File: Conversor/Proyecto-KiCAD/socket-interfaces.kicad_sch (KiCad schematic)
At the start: 24 parts, among them J7 DIMM100, P10 Header GPIO, P11 Header SD, P5 Header 7X2, P6 Header UART, P7 Header I2C, P8 Header PWM, P9 Header ADC, SW1 Switch, SW2 Switch, SW3 Switch, SW4 Switch

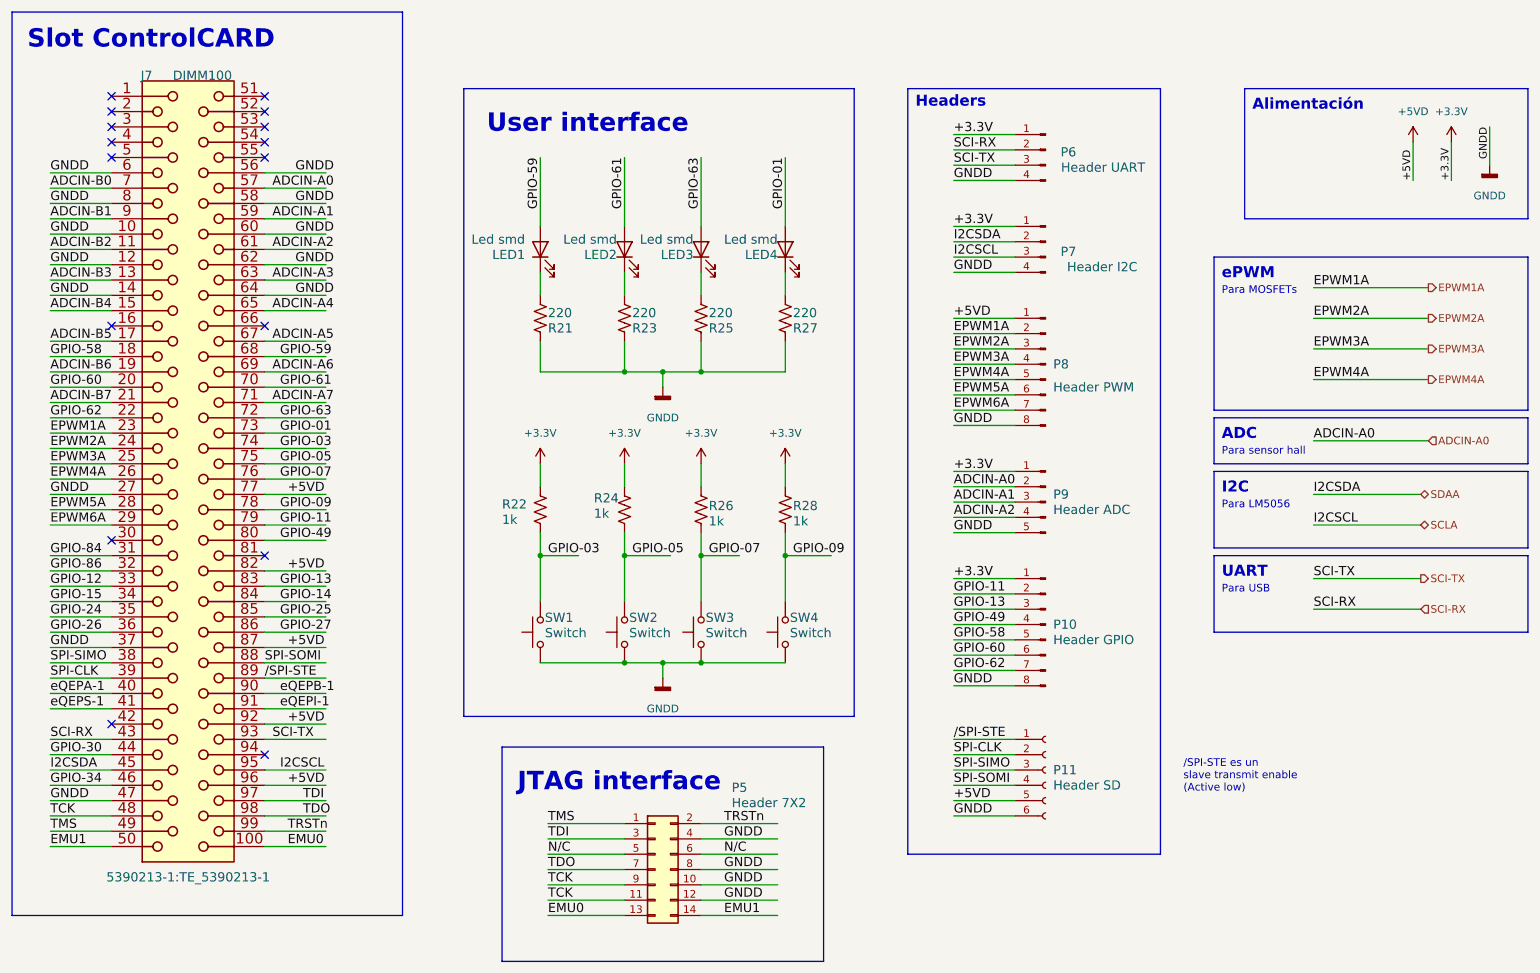
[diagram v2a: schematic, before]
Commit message: Reempezar el ordenado de componentes del PCB
- Intentar copiar mas a la placa adaptadora en la parte del DSP (digital)
  - Algunas cosas (como los headers y la parte de USB) se movieron para hacer entrar mejor las cosas
- Layout bastante completo
- Agregados algunos modelos 3D faltantes
Por hacer:
  - Mover y reorganizar la parte del LM5056, porque tiene una pata que va al secundario, y ahora esta muy lejos del area de GND2
  - Ver como reorganizar un poco para que no queden esquinas vacias
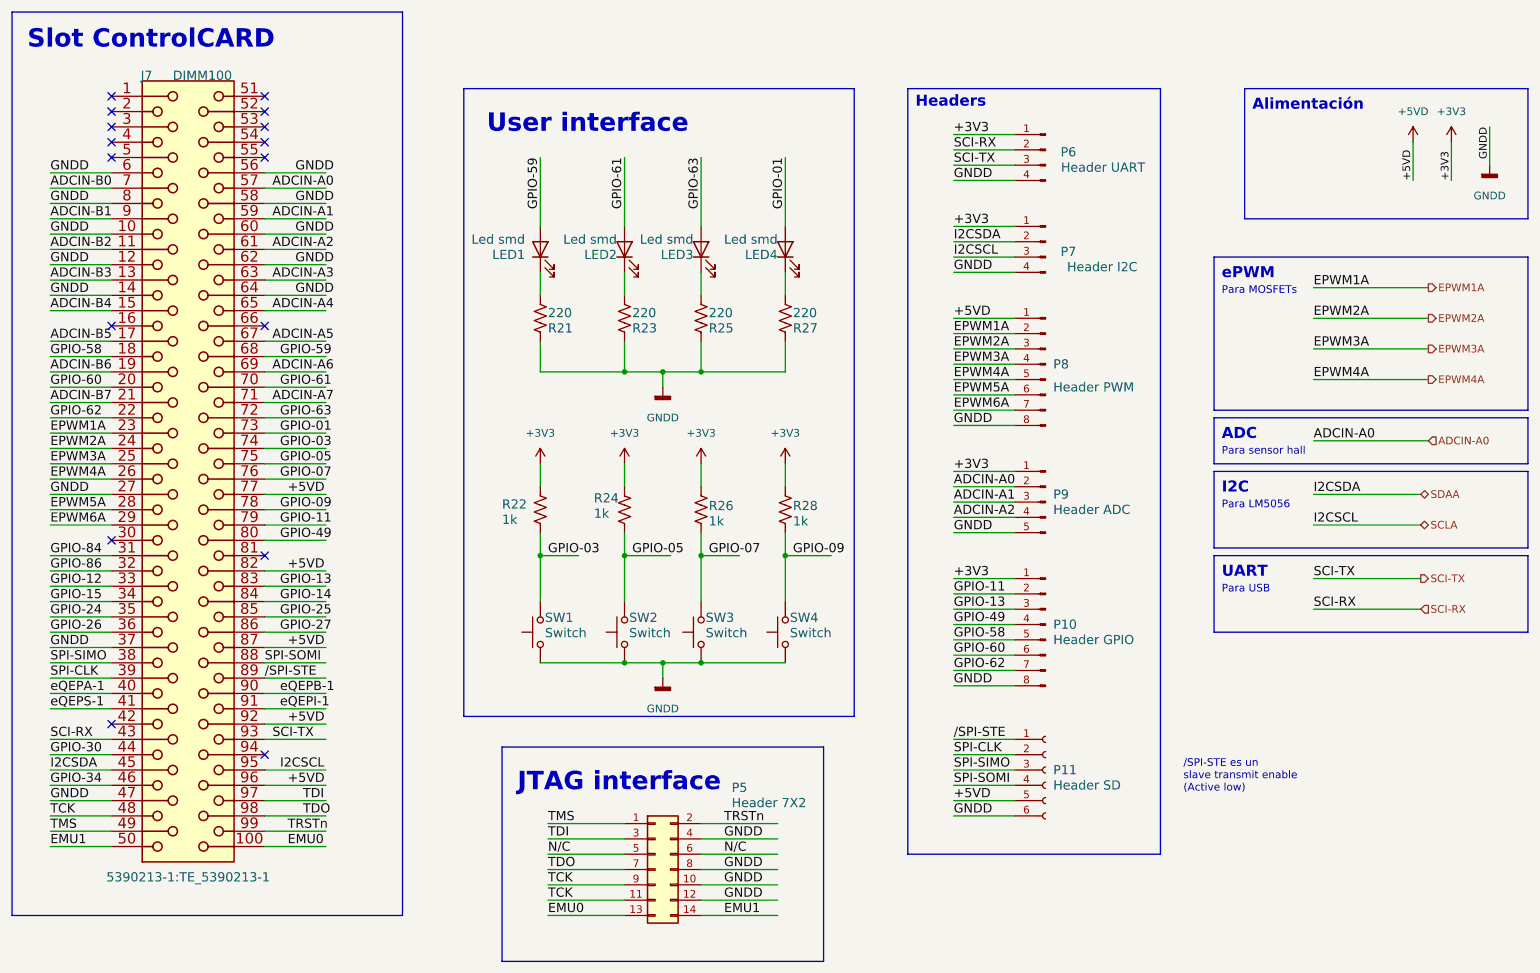
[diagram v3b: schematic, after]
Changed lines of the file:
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@@
     (effects (font (size 1.524 1.524)) (justify left bottom))
   )
-  (label "+3.3V" (at 175.26 91.44 0)
+  (label "+3V3" (at 175.26 91.44 0)
     (effects (font (size 1.524 1.524)) (justify left bottom))
   )
@@
     (effects (font (size 1.524 1.524)) (justify left bottom))
   )
-  (label "+3.3V" (at 175.26 35.56 0)
+  (label "+3V3" (at 175.26 35.56 0)
     (effects (font (size 1.524 1.524)) (justify left bottom))
   )
@@
     (effects (font (size 1.524 1.524)) (justify left bottom))
   )
-  (label "+3.3V" (at 175.26 109.22 0)
+  (label "+3V3" (at 175.26 109.22 0)
     (effects (font (size 1.524 1.524)) (justify left bottom))
   )
@@
     (effects (font (size 1.524 1.524)) (justify left bottom))
   )
-  (label "+3.3V" (at 257.81 43.18 90)
+  (label "+3V3" (at 257.81 43.18 90)
     (effects (font (size 1.27 1.27)) (justify left bottom))
   )
@@
     (effects (font (size 1.524 1.524)) (justify left bottom))
   )
-  (label "+3.3V" (at 175.26 50.8 0)
+  (label "+3V3" (at 175.26 50.8 0)
     (effects (font (size 1.524 1.524)) (justify left bottom))
   )
@@
     (effects (font (size 1.27 1.27)) (justify left))
   )
+  (symbol (lib_id "power:+3V3") (at 133.35 90.17 0) (unit 1)
+    (in_bom yes) (on_board yes) (fields_autoplaced)
+    (property "Reference" "#PWR0119" (id 0) (at 133.35 93.98 0)
+      (effects (font (size 1.27 1.27)) hide)
+    )
+    (property "Value" "+3V3" (id 1) (at 133.35 85.09 0))
+    (property "Footprint" "" (id 2) (at 133.35 90.17 0)
+      (effects (font (size 1.27 1.27)) hide)
+    )
+    (property "Datasheet" "" (id 3) (at 133.35 90.17 0)
+      (effects (font (size 1.27 1.27)) hide)
+    )
+    (pin "1")
+  )
   (symbol (lib_id "Device:R_US") (at 133.35 97.79 180) (unit 1)
     (in_bom yes) (on_board yes)
@@
     (pin "2")
   )
-  (symbol (lib_id "power:+3.3V") (at 120.65 90.17 0) (unit 1)
+  (symbol (lib_id "power:+3V3") (at 120.65 90.17 0) (unit 1)
     (in_bom yes) (on_board yes) (fields_autoplaced)
-    (property "Reference" "#PWR0121" (id 0) (at 120.65 93.98 0)
-      (effects (font (size 1.27 1.27)) hide)
-    )
-    (property "Value" "+3.3V" (id 1) (at 120.65 85.09 0))
+    (property "Reference" "#PWR0144" (id 0) (at 120.65 93.98 0)
+      (effects (font (size 1.27 1.27)) hide)
+    )
+    (property "Value" "+3V3" (id 1) (at 120.65 85.09 0))
     (property "Footprint" "" (id 2) (at 120.65 90.17 0)
       (effects (font (size 1.27 1.27)) hide)
@@
     (pin "9")
   )
+  (symbol (lib_id "power:+3V3") (at 147.32 90.17 0) (unit 1)
+    (in_bom yes) (on_board yes) (fields_autoplaced)
+    (property "Reference" "#PWR0121" (id 0) (at 147.32 93.98 0)
+      (effects (font (size 1.27 1.27)) hide)
+    )
+    (property "Value" "+3V3" (id 1) (at 147.32 85.09 0))
+    (property "Footprint" "" (id 2) (at 147.32 90.17 0)
+      (effects (font (size 1.27 1.27)) hide)
+    )
+    (property "Datasheet" "" (id 3) (at 147.32 90.17 0)
+      (effects (font (size 1.27 1.27)) hide)
+    )
+    (pin "1")
+  )
   (symbol (lib_id "Device:R_US") (at 106.68 66.04 0) (unit 1)
     (in_bom yes) (on_board yes)
@@
     (pin "1")
     (pin "2")
-  )
-  (symbol (lib_id "power:+3.3V") (at 106.68 90.17 0) (unit 1)
-    (in_bom yes) (on_board yes) (fields_autoplaced)
-    (property "Reference" "#PWR0122" (id 0) (at 106.68 93.98 0)
-      (effects (font (size 1.27 1.27)) hide)
-    )
-    (property "Value" "+3.3V" (id 1) (at 106.68 85.09 0))
-    (property "Footprint" "" (id 2) (at 106.68 90.17 0)
-      (effects (font (size 1.27 1.27)) hide)
-    )
-    (property "Datasheet" "" (id 3) (at 106.68 90.17 0)
-      (effects (font (size 1.27 1.27)) hide)
-    )
-    (pin "1")
   )
   (symbol (lib_id "Connector:Conn_01x06_Female") (at 190.5 140.97 0) (unit 1)
@@
     (pin "1")
   )
-  (symbol (lib_id "power:+3.3V") (at 147.32 90.17 0) (unit 1)
-    (in_bom yes) (on_board yes) (fields_autoplaced)
-    (property "Reference" "#PWR0118" (id 0) (at 147.32 93.98 0)
-      (effects (font (size 1.27 1.27)) hide)
-    )
-    (property "Value" "+3.3V" (id 1) (at 147.32 85.09 0))
-    (property "Footprint" "" (id 2) (at 147.32 90.17 0)
-      (effects (font (size 1.27 1.27)) hide)
-    )
-    (property "Datasheet" "" (id 3) (at 147.32 90.17 0)
-      (effects (font (size 1.27 1.27)) hide)
-    )
-    (pin "1")
-  )
   (symbol (lib_id "Switch:SW_Push") (at 106.68 118.11 90) (unit 1)
     (in_bom yes) (on_board yes)
@@
     (pin "1")
     (pin "2")
-  )
-  (symbol (lib_id "power:+3.3V") (at 133.35 90.17 0) (unit 1)
-    (in_bom yes) (on_board yes) (fields_autoplaced)
-    (property "Reference" "#PWR0119" (id 0) (at 133.35 93.98 0)
-      (effects (font (size 1.27 1.27)) hide)
-    )
-    (property "Value" "+3.3V" (id 1) (at 133.35 85.09 0))
-    (property "Footprint" "" (id 2) (at 133.35 90.17 0)
-      (effects (font (size 1.27 1.27)) hide)
-    )
-    (property "Datasheet" "" (id 3) (at 133.35 90.17 0)
-      (effects (font (size 1.27 1.27)) hide)
-    )
-    (pin "1")
   )
   (symbol (lib_id "Connector:Conn_01x08_Male") (at 190.5 116.84 0) (mirror y) (unit 1)
@@
     (pin "1")
   )
+  (symbol (lib_id "power:+3V3") (at 106.68 90.17 0) (unit 1)
+    (in_bom yes) (on_board yes) (fields_autoplaced)
+    (property "Reference" "#PWR0122" (id 0) (at 106.68 93.98 0)
+      (effects (font (size 1.27 1.27)) hide)
+    )
+    (property "Value" "+3V3" (id 1) (at 106.68 85.09 0))
+    (property "Footprint" "" (id 2) (at 106.68 90.17 0)
+      (effects (font (size 1.27 1.27)) hide)
+    )
+    (property "Datasheet" "" (id 3) (at 106.68 90.17 0)
+      (effects (font (size 1.27 1.27)) hide)
+    )
+    (pin "1")
+  )
   (symbol (lib_id "Device:LED") (at 106.68 54.61 90) (unit 1)
     (in_bom yes) (on_board yes)
@@
     (pin "2")
   )
-  (symbol (lib_id "power:+3.3V") (at 257.81 36.83 0) (unit 1)
+  (symbol (lib_id "power:+3V3") (at 257.81 36.83 0) (unit 1)
     (in_bom yes) (on_board yes) (fields_autoplaced)
-    (property "Reference" "#PWR0116" (id 0) (at 257.81 40.64 0)
-      (effects (font (size 1.27 1.27)) hide)
-    )
-    (property "Value" "+3.3V" (id 1) (at 257.81 31.75 0))
+    (property "Reference" "#PWR0118" (id 0) (at 257.81 40.64 0)
+      (effects (font (size 1.27 1.27)) hide)
+    )
+    (property "Value" "+3V3" (id 1) (at 257.81 31.75 0))
     (property "Footprint" "" (id 2) (at 257.81 36.83 0)
       (effects (font (size 1.27 1.27)) hide)

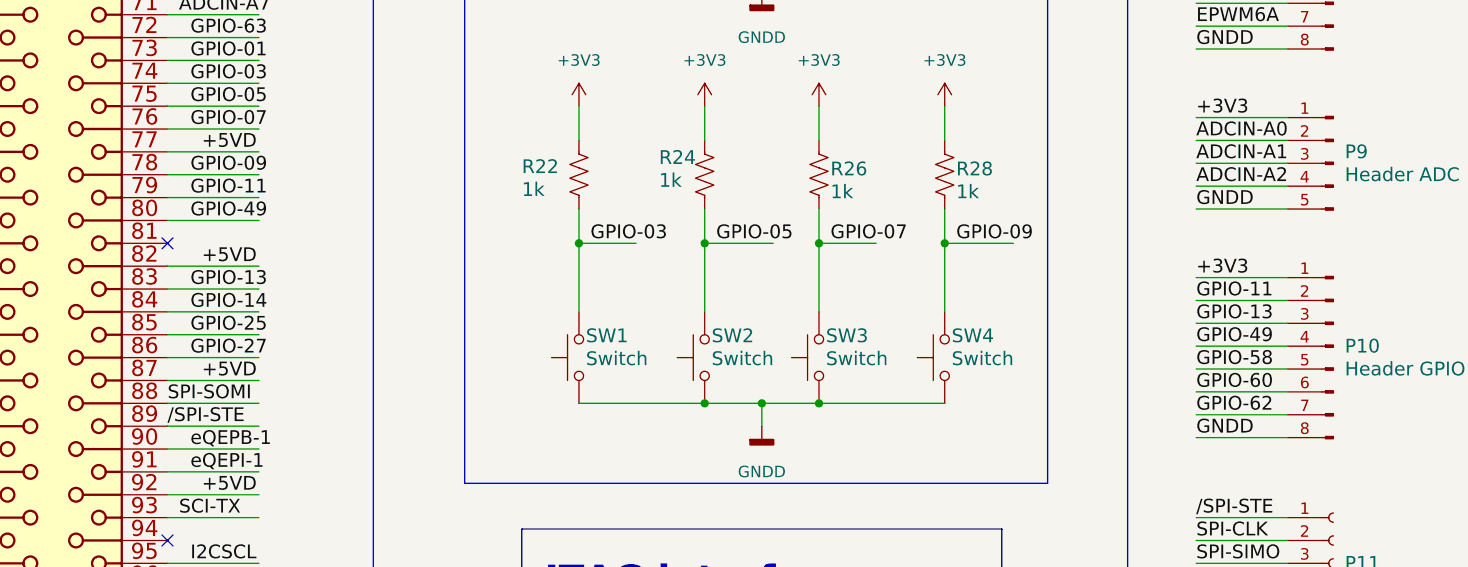
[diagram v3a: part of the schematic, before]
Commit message: Terminar la parte digital de la PCB (incluidas las pistas)
- Hay que ver si la clearance de 0.254mm para el plano de GNDD esta bien
- Cambiar la footprint del FTDI por la version correcta
- Borrar R37, R38 y R39 (usadas para corregir errores del ERC)
Por hacer:
  - Terminar las otras dos partes de la placa
  - Consultar si esta bien lo que hice hasta ahora
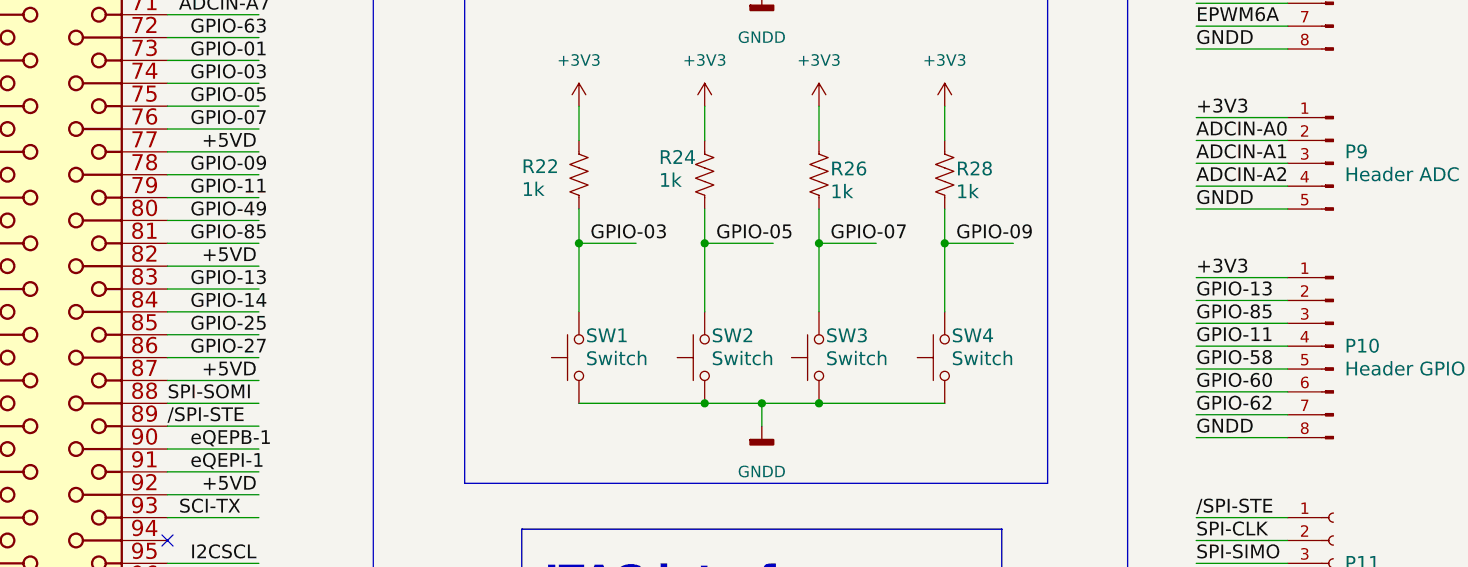
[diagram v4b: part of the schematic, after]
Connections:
- net GPIO-11: now also P10.4 (Pin_4); no longer P10.2 (Pin_2)
- net GPIO-13: now also P10.2 (Pin_2); no longer P10.3 (Pin_3)
- net GPIO-49: no longer P10.4 (Pin_4)
- net GPIO-85: now reaches J7.81 (p81)
- net GPIO-85: now also P10.3 (Pin_3)
- no-connect marks 16 -> 15
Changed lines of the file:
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@@
   (no_connect (at 35.56 31.75))
   (no_connect (at 60.96 29.21))
-  (no_connect (at 60.96 105.41))
   (no_connect (at 60.96 36.83))
   (no_connect (at 60.96 39.37))
@@
     (stroke (width 0) (type default) (color 0 0 0 0))
   )
+  (wire (pts (xy 60.96 105.41) (xy 71.12 105.41))
+    (stroke (width 0) (type default) (color 0 0 0 0))
+  )
   (wire (pts (xy 25.4 100.33) (xy 35.56 100.33))
     (stroke (width 0) (type default) (color 0 0 0 0))
@@
     (effects (font (size 1.524 1.524)) (justify left bottom))
   )
-  (label "GPIO-49" (at 175.26 116.84 0)
+  (label "GPIO-11" (at 175.26 116.84 0)
     (effects (font (size 1.524 1.524)) (justify left bottom))
   )
@@
   )
   (label "GNDD" (at 66.04 46.99 0)
+    (effects (font (size 1.524 1.524)) (justify left bottom))
+  )
+  (label "GPIO-85" (at 63.5 105.41 0)
     (effects (font (size 1.524 1.524)) (justify left bottom))
   )
@@
     (effects (font (size 1.524 1.524)) (justify left bottom))
   )
-  (label "GPIO-13" (at 175.26 114.3 0)
+  (label "GPIO-85" (at 175.26 114.3 0)
     (effects (font (size 1.524 1.524)) (justify left bottom))
   )
@@
     (effects (font (size 1.524 1.524)) (justify left bottom))
   )
-  (label "GPIO-11" (at 175.26 111.76 0)
-    (effects (font (size 1.524 1.524)) (justify left bottom))
-  )
+  (label "GPIO-13" (at 175.26 111.76 0)
+    (effects (font (size 1.524 1.524)) (justify left bottom))
+  )
